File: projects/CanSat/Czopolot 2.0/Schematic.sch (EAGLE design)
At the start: 112 parts

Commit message: VERSION 1.0.0
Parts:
- removed C19: 100n, Unified:CAPACITOR0603
- removed U$21, U$22, U$23, U$24, U$25, U$26, U$27, U$28: PAD, Unified:PAD
- removed U$29, U$31, U$32: PADRND, Unified:PADRND
- removed U$30, U$33, U$34: PADOCT, Unified:PADOCT
- added P1, P2, P3, P4: PADBIG, Unified:PADBIG
- added R9: VBACK_CH, Unified:RESISTOR0603
- added U$16: SUPCAP, SobieskiSat2:SUPCAP
- C16: device Unified:CAPACITOR0603 -> Unified:CAPACITOR1206
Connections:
- removed net N$43: U$1STM32F405RGT6_GPIO.PC0, U$21.1
- removed net N$44: U$1STM32F405RGT6_GPIO.PC1, U$22.1
- removed net N$45: U$1STM32F405RGT6_GPIO.PC2, U$23.1
- removed net N$46: U$1STM32F405RGT6_GPIO.PC3, U$24.1
- removed net N$47: U$1STM32F405RGT6_GPIO.PB0, U$25.1
- removed net N$48: U$1STM32F405RGT6_GPIO.PB1, U$26.1
- removed net N$50: U$1STM32F405RGT6_GPIO.PC5, U$28.1
- new net H1: U$13.P$3, U$1STM32F405RGT6_GPIO.PC1
- new net H2: U$13.P$4, U$1STM32F405RGT6_GPIO.PC3
- new net H4: U$13.P$6, U$1STM32F405RGT6_GPIO.PB1
- new net P1: P1.1, U$1STM32F405RGT6_GPIO.PC0
- new net P2: P2.1, U$1STM32F405RGT6_GPIO.PC2
- new net P3: P3.1, U$1STM32F405RGT6_GPIO.PB0
- new net P4: P4.1, U$1STM32F405RGT6_GPIO.PC5
- net DAC: now also U$13.P$5; no longer U$27.1
- net GND: now also U$13.P$2, U$13.P$7, U$16.2; no longer C19.2, U$30.1, U$33.1, U$34.1
- net N$20: now also U$1STM32F405RGT6_GPIO.PB13; no longer U$1STM32F405RGT6_GPIO.PB15
- net VBACKUP: now also R9.1, U$16.1
- net VCC: now also R9.2; no longer C19.1, U$29.1, U$32.1
- net VSYS: now also U$13.P$1, U$13.P$8; no longer U$31.1
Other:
- moved on the sheet: D8, RN1C

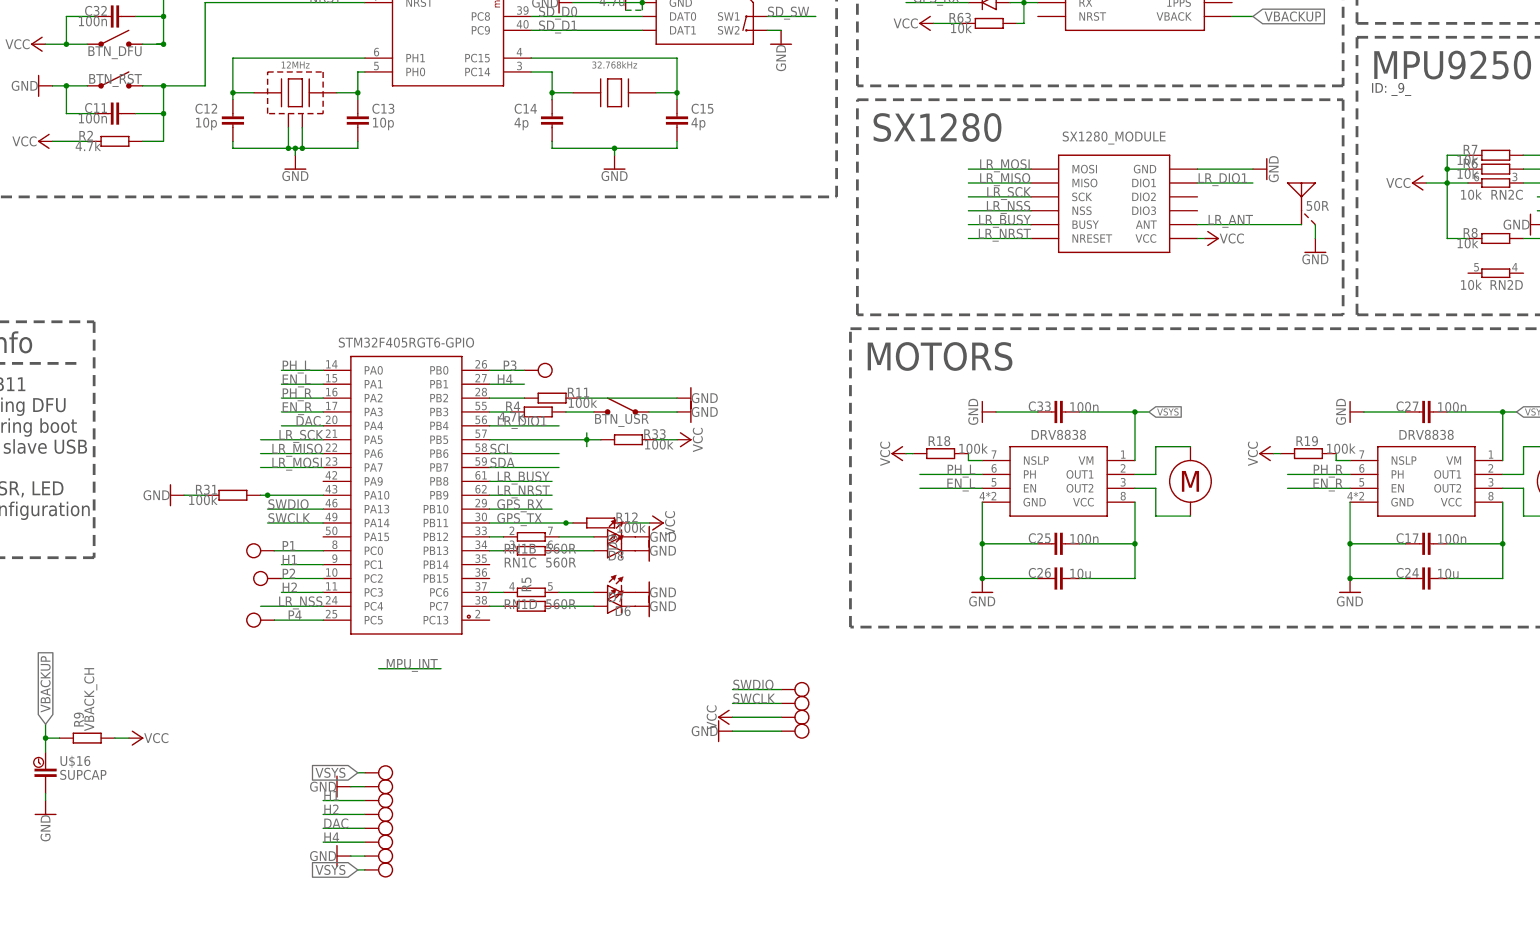
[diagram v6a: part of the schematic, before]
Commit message: 433MHz support added
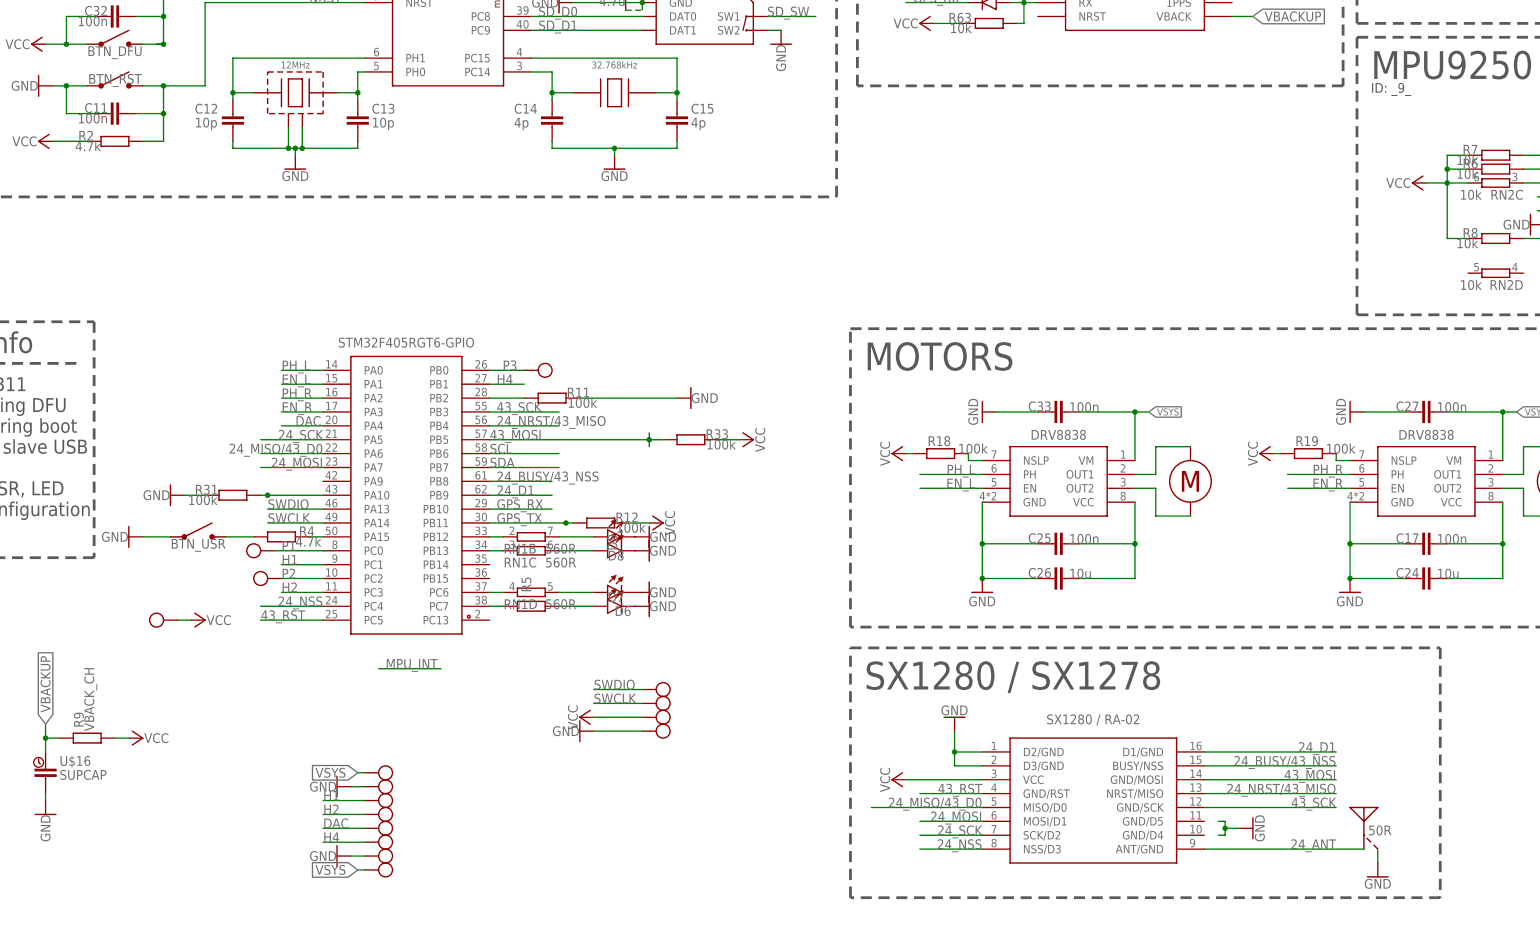
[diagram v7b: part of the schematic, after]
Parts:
- removed U$4: SX1280, SobieskiSat2:SX1280
- added U$21: LORADUO, SobieskiSat2:LORADUO
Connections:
- removed net LR_ANT: U$12.SIG, U$4.ANT
- removed net LR_BUSY: U$1STM32F405RGT6_GPIO.PB8, U$4.BUSY
- removed net LR_DIO1: U$1STM32F405RGT6_GPIO.PB4, U$4.DIO1
- removed net LR_MISO: U$1STM32F405RGT6_GPIO.PA6, U$4.MISO
- removed net LR_MOSI: U$1STM32F405RGT6_GPIO.PA7, U$4.MOSI
- removed net LR_NRST: U$1STM32F405RGT6_GPIO.PB9, U$4.NRESET
- removed net LR_NSS: U$1STM32F405RGT6_GPIO.PC4, U$4.NSS
- removed net LR_SCK: U$1STM32F405RGT6_GPIO.PA5, U$4.SCK
- removed net N$51: R33.2, U$1STM32F405RGT6_GPIO.PB5
- removed net P4: P4.1, U$1STM32F405RGT6_GPIO.PC5
- new net 24_ANT: U$12.SIG, U$21.ANT/GND
- new net 24_BUSY/43_NSS: U$1STM32F405RGT6_GPIO.PB8, U$21.BUSY/NSS
- new net 24_D1: U$1STM32F405RGT6_GPIO.PB9, U$21.D1/GND
- new net 24_MISO/43_D0: U$1STM32F405RGT6_GPIO.PA6, U$21.MISO/D0
- new net 24_MOSI: U$1STM32F405RGT6_GPIO.PA7, U$21.MOSI/D1
- new net 24_NRST/43_MISO: U$1STM32F405RGT6_GPIO.PB4, U$21.NRST/MISO
- new net 24_NSS: U$1STM32F405RGT6_GPIO.PC4, U$21.NSS/D3
- new net 24_SCK: U$1STM32F405RGT6_GPIO.PA5, U$21.SCK/D2
- new net 43_MOSI: R33.2, U$1STM32F405RGT6_GPIO.PB5, U$21.GND/MOSI
- new net 43_RST: U$1STM32F405RGT6_GPIO.PC5, U$21.GND/RST
- new net 43_SCK: U$1STM32F405RGT6_GPIO.PB3, U$21.GND/SCK
- net GND: now also U$21.D2/GND, U$21.D3/GND; no longer U$4.GND
- net N$4: now also U$1STM32F405RGT6_GPIO.PA15; no longer U$1STM32F405RGT6_GPIO.PB3
- net VCC: now also P4.1, U$21.VCC; no longer U$4.VCC
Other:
- note added: "SX1280 / SX1278"
- note removed: "SX1280"
- moved on the sheet: BTN_USR, R33, R4

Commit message: Schematic updated for CDR
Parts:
- RN1, RN2: device resistor-dil:4R-NEXB38V -> SobieskiSat2:RESISTORARRAY
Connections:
- removed net MPU_INT: U$9.INT
- net BMP_SDI: now also RN2G$1.1; no longer RN2A.1
- net BMP_SDO: now also RN2G$2.2; no longer RN2B.2
- net GND: now also RN2G$2.1; no longer RN2B.1
- net MPU_NCS: now also RN2G$3.1; no longer RN2C.1
- net N$1: now also RN1G$2.2; no longer RN1B.2
- net N$10: now also RN1G$1.1; no longer RN1A.1
- net N$19: now also RN1G$4.1; no longer RN1D.1
- net N$2: now also RN1G$3.2; no longer RN1C.2
- net N$20: now also RN1G$3.1; no longer RN1C.1
- net N$28: now also RN1G$2.1; no longer RN1B.1
- net N$3: now also RN1G$1.2; no longer RN1A.2
- net N$37: now also RN1G$4.2; no longer RN1D.2
- net VCC: now also RN2G$1.2, RN2G$3.2; no longer RN2A.2, RN2C.2
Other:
- note added: "Battery management - BQ24253"
- note added: "GPS - PA6H (MT3339)"
- note added: "IMU - MPU9250"
- note added: "MCU Power"
- note added: "MCU Utilities"
- note added: "Motor drivers - DRV8838"
- note added: "Pressure sensor"
- note added: "Radio - SX1280 or SX1278"
- note added: "Voltage regulator - 3.3V"
- note removed: "4.7u was there"
- note removed: "BMP280"
- note removed: "BQ24253"
- note removed: "GPS"
- note removed: "ID: _2_"
- note removed: "ID: _6_"
- note removed: "ID: _9_"
- note removed: "MCU_POWER"
- note removed: "MCU_UTILITIES"
- note removed: "MOTORS"
- note removed: "MPU9250"
- note removed: "REGULATOR"
- note removed: "SX1280 / SX1278"
- moved on the sheet: BAT_PACK, BTN_DFU, BTN_RST, BTN_USR, C1, C10, C11, C12, C13, C14, C15, C16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
